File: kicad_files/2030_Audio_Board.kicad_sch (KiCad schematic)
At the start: 18 parts

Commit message: pcb updated
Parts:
- added H1: HSE-B20254-035H-01, HSEB20254035H01, symbol SamacSys_Parts:HSE-B20254-035H-01
- C1: renamed from C?; footprint (none) -> Capacitor_THT:CP_Radial_D8.0mm_P5.00mm
- C2: renamed from C?; footprint (none) -> Capacitor_THT:CP_Radial_D10.0mm_P5.00mm
- C3, C5, C6: renamed from C?; footprint (none) -> Capacitor_SMD:C_0603_1608Metric_Pad1.08x0.95mm_HandSolder
- C4: renamed from C?; footprint (none) -> Capacitor_SMD:C_0805_2012Metric_Pad1.18x1.45mm_HandSolder
- C7: renamed from C?; footprint (none) -> Capacitor_THT:CP_Radial_D12.5mm_P5.00mm
- LS1: renamed from LS?; footprint (none) -> footprints:JST_B2B-PH-K-S(LF)(SN)
- R1, R2, R3, R4, R5: renamed from R?; footprint (none) -> Resistor_SMD:R_0603_1608Metric_Pad0.98x0.95mm_HandSolder
- R6: renamed from R?; footprint (none) -> Resistor_SMD:R_1206_3216Metric_Pad1.30x1.75mm_HandSolder
- RV1: renamed from RV?; footprint (none) -> Potentiometer_THT:Potentiometer_Piher_T-16H_Single_Horizontal
- gave numbers to parts that had none: 3
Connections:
- net -12V: now also H1.1, H1.2

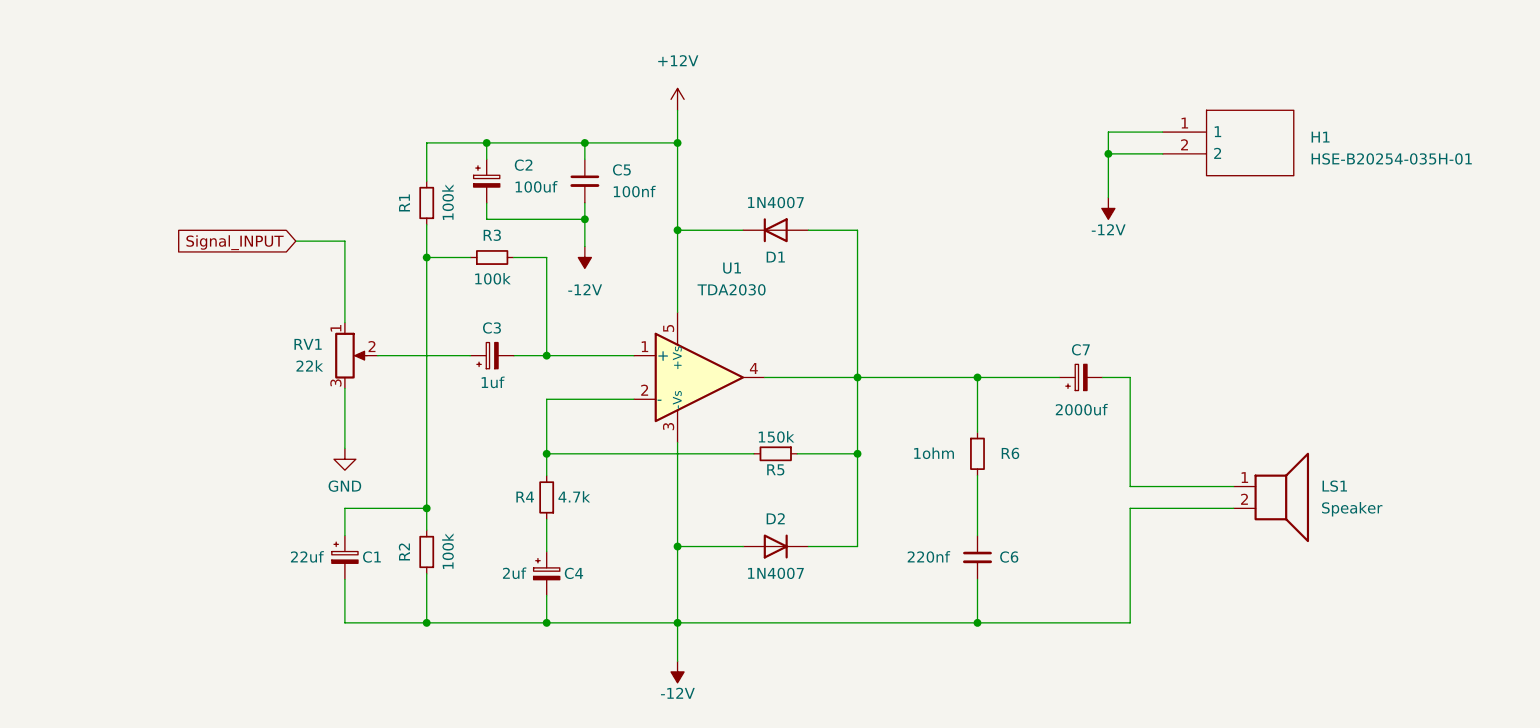
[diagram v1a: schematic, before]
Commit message: routing completed in single layer
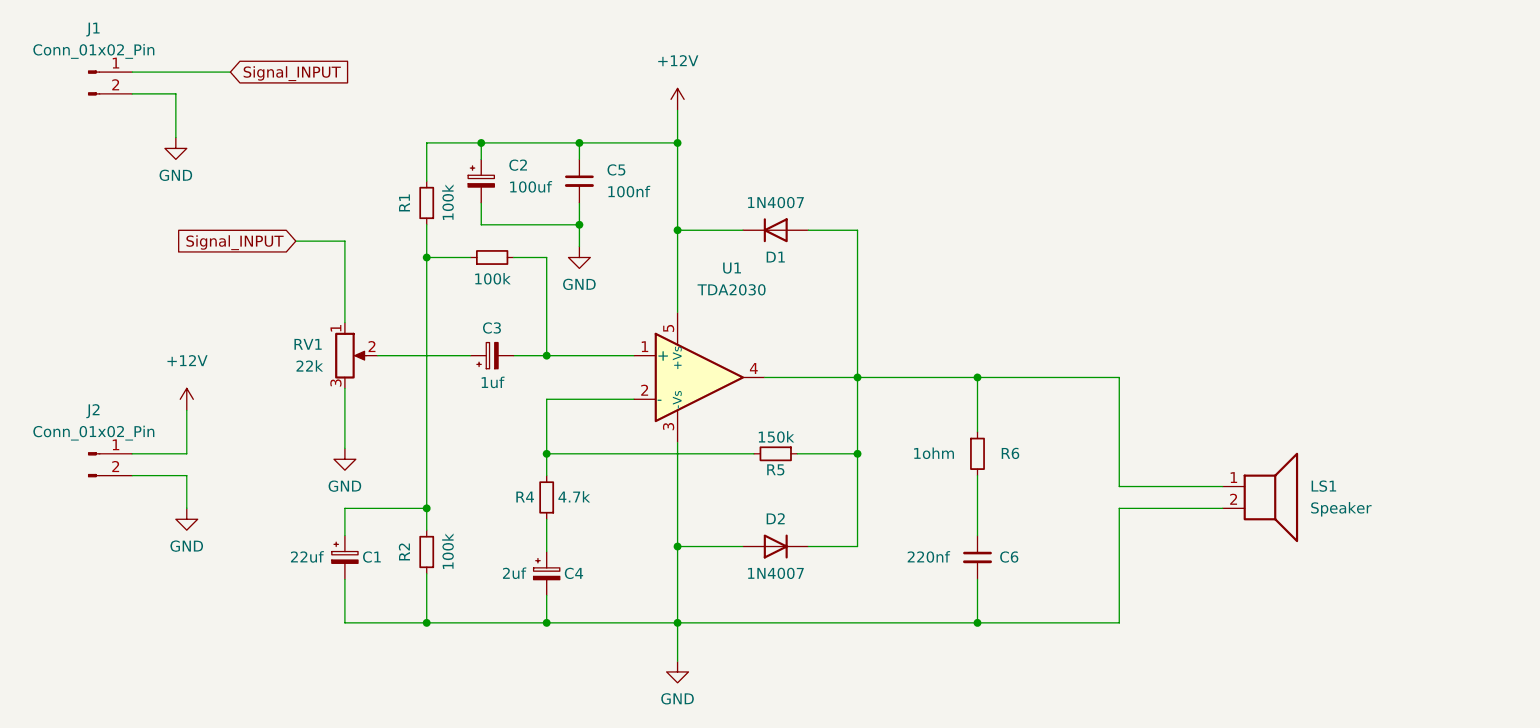
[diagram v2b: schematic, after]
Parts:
- removed C7: 2000uf, Capacitor_THT:CP_Radial_D12.5mm_P5.00mm, symbol Device:C_Polarized_Small
- removed H1: HSE-B20254-035H-01, HSEB20254035H01, symbol SamacSys_Parts:HSE-B20254-035H-01
- added J1, J2: Conn_01x02_Pin, footprints:JST_B2B-PH-K-S(LF)(SN), symbol Connector:Conn_01x02_Pin
- C3, C5, C6: footprint Capacitor_SMD:C_0603_1608Metric_Pad1.08x0.95mm_HandSolder -> Capacitor_THT:C_Disc_D4.3mm_W1.9mm_P5.00mm
- C4: footprint Capacitor_SMD:C_0805_2012Metric_Pad1.18x1.45mm_HandSolder -> Capacitor_THT:C_Disc_D4.3mm_W1.9mm_P5.00mm
- R1, R2, R3, R4, R5: footprint Resistor_SMD:R_0603_1608Metric_Pad0.98x0.95mm_HandSolder -> Resistor_THT:R_Axial_DIN0204_L3.6mm_D1.6mm_P7.62mm_Horizontal
- R6: footprint Resistor_SMD:R_1206_3216Metric_Pad1.30x1.75mm_HandSolder -> Resistor_THT:R_Axial_DIN0204_L3.6mm_D1.6mm_P7.62mm_Horizontal
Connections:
- net -12V is gone; now on net GND: C1.2, C2.2, C4.2, C5.2, C6.2, D2.2 (A), LS1.2, R2.1, U1.3 (-Vs)
- net +12V: now also J2.1 (Pin_1)
- net GND: now also J1.2 (Pin_2), J2.2 (Pin_2)
- net Signal_INPUT: now also J1.1 (Pin_1)
- net at D1.2 (A), D2.1 (K), R5.1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: now also LS1.1
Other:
- company: SPECIFIC_ELECTRONICS -> (none)
- moved on the sheet: C2, C5, LS1
